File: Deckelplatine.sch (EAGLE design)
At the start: 64 parts, among them IC1 MAX1487EESA+, IC2 74HCT595D, IC3 74HCT595D, IC4 74HCT595D, IC5 74HCT595D, IC6 74HCT595D, J1 52808-2570, U1 LM2676S, X1 236-406/000-023, X2 233-502

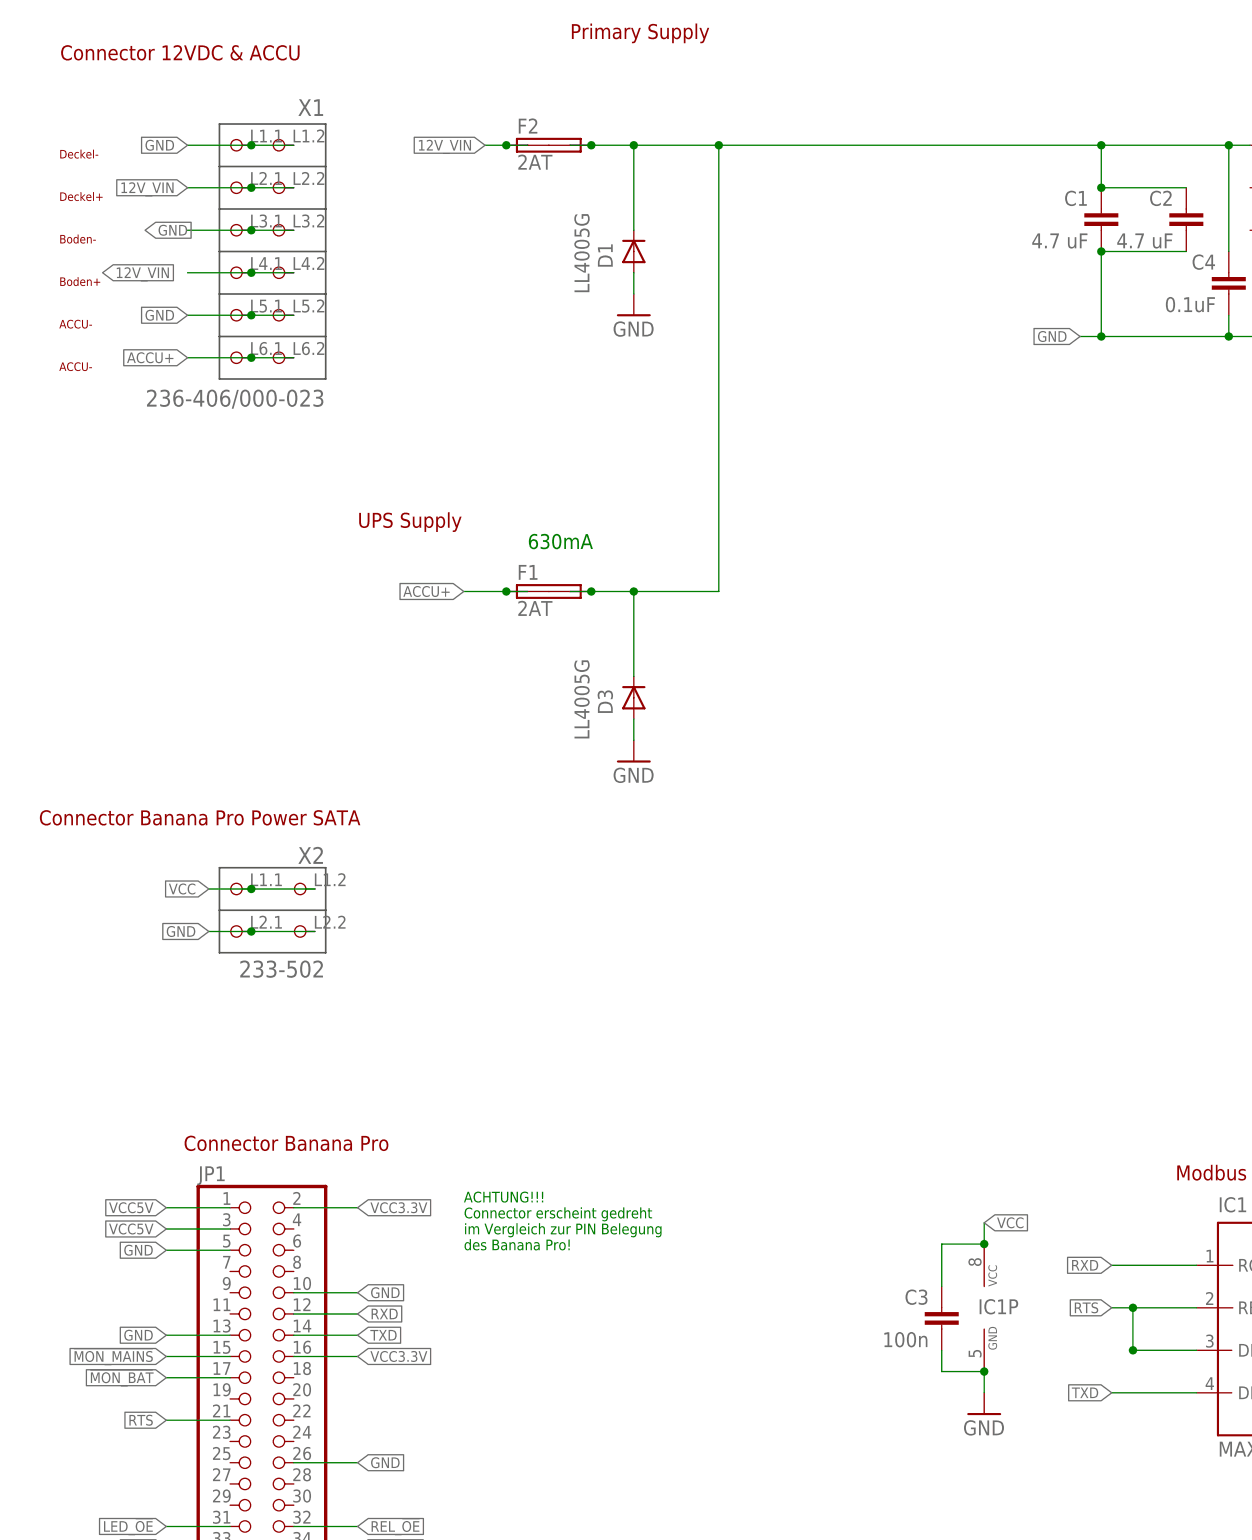
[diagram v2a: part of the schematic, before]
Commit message: BAT und MAINS Monitor
Konnectoren in eigener Bibliothek 'Deckelplatine.lbr'
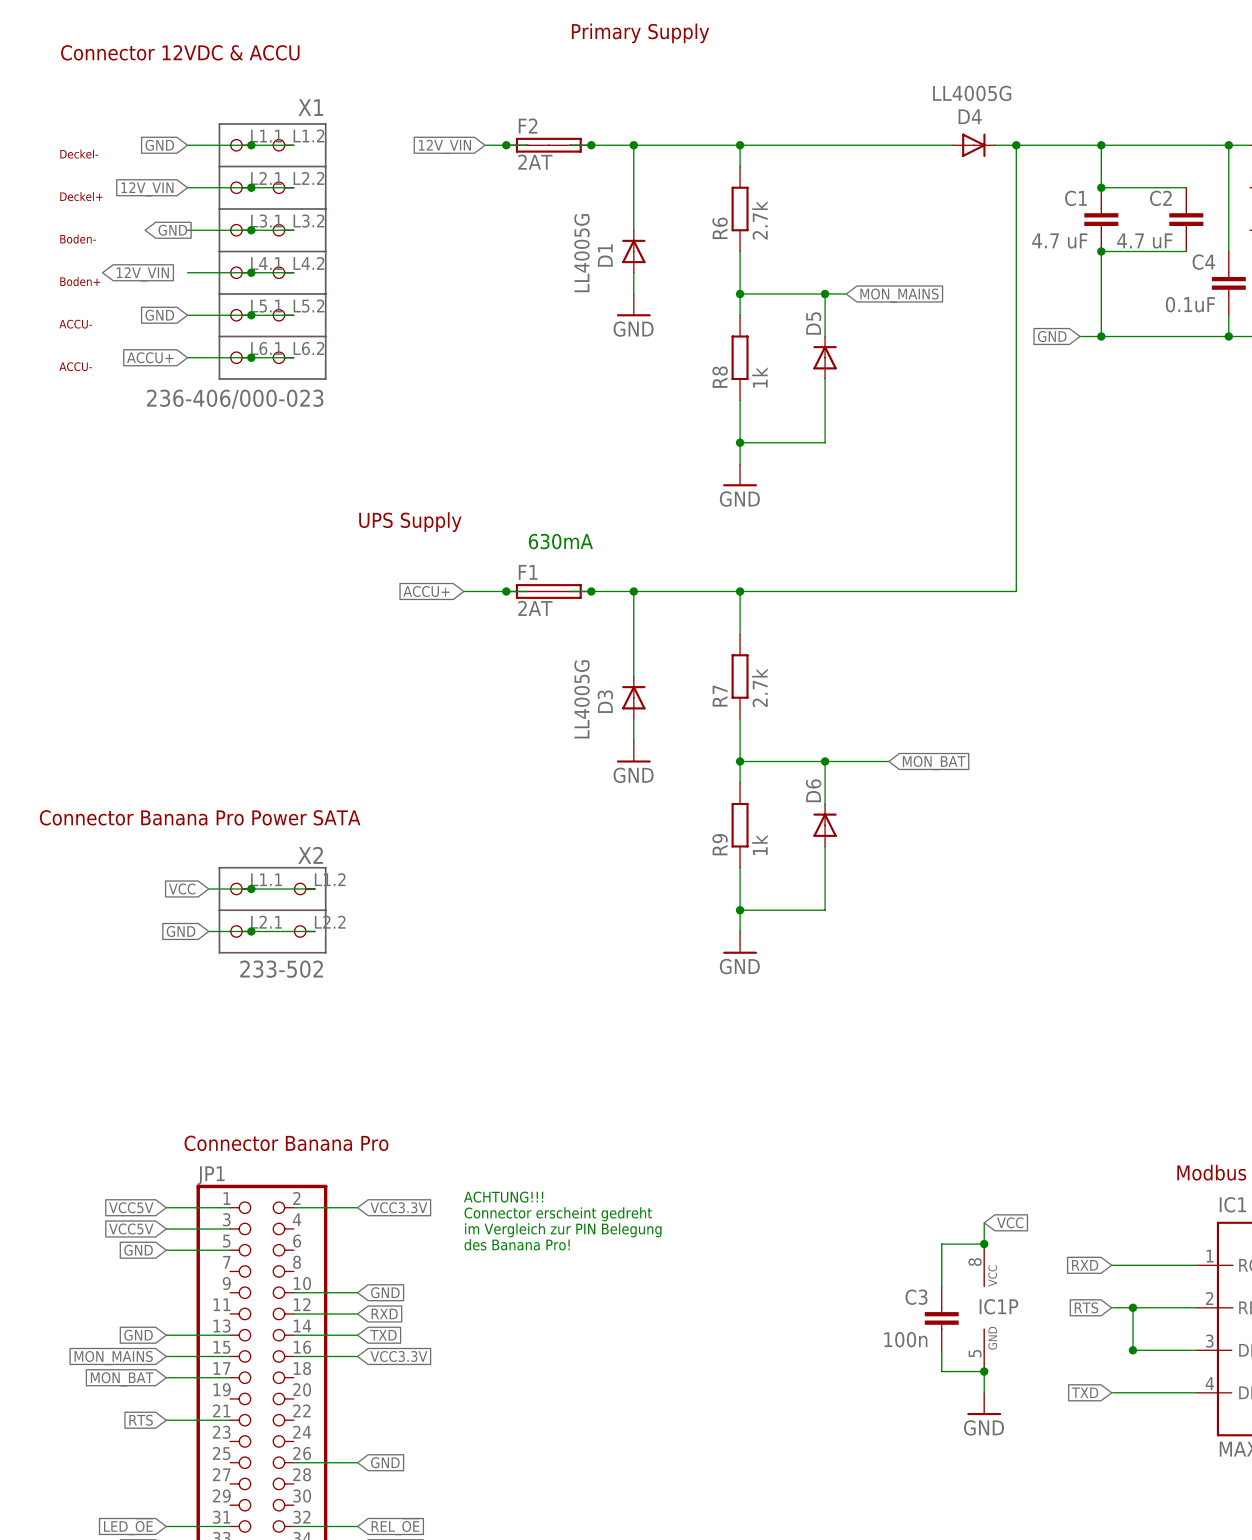
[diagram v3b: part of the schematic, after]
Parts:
- added D4: LL4005G, diode:DIODE-MELF-MLL41
- added D5, D6: (no value), Deckelplatine:DIODE-SOD523
- added R6, R7: 2.7k, RA-GAS Projekte LTD:R-EU_R0603
- added R8, R9: 1k, RA-GAS Projekte LTD:R-EU_R0603
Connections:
- removed net !MON_BAT: JP1.17
- removed net !MON_MAINS: JP1.15
- new net MON_BAT: D6.C, JP1.17, R7.1, R9.2
- new net MON_MAINS: D5.C, JP1.15, R6.1, R8.2
- new net N$37: D1.C, D4.A, F2.2A, F2.2B, R6.2
- net GND: now also D5.A, D6.A, R8.1, R9.1
- net N$4: now also D4.C, R7.2; no longer D1.C, F2.2A, F2.2B

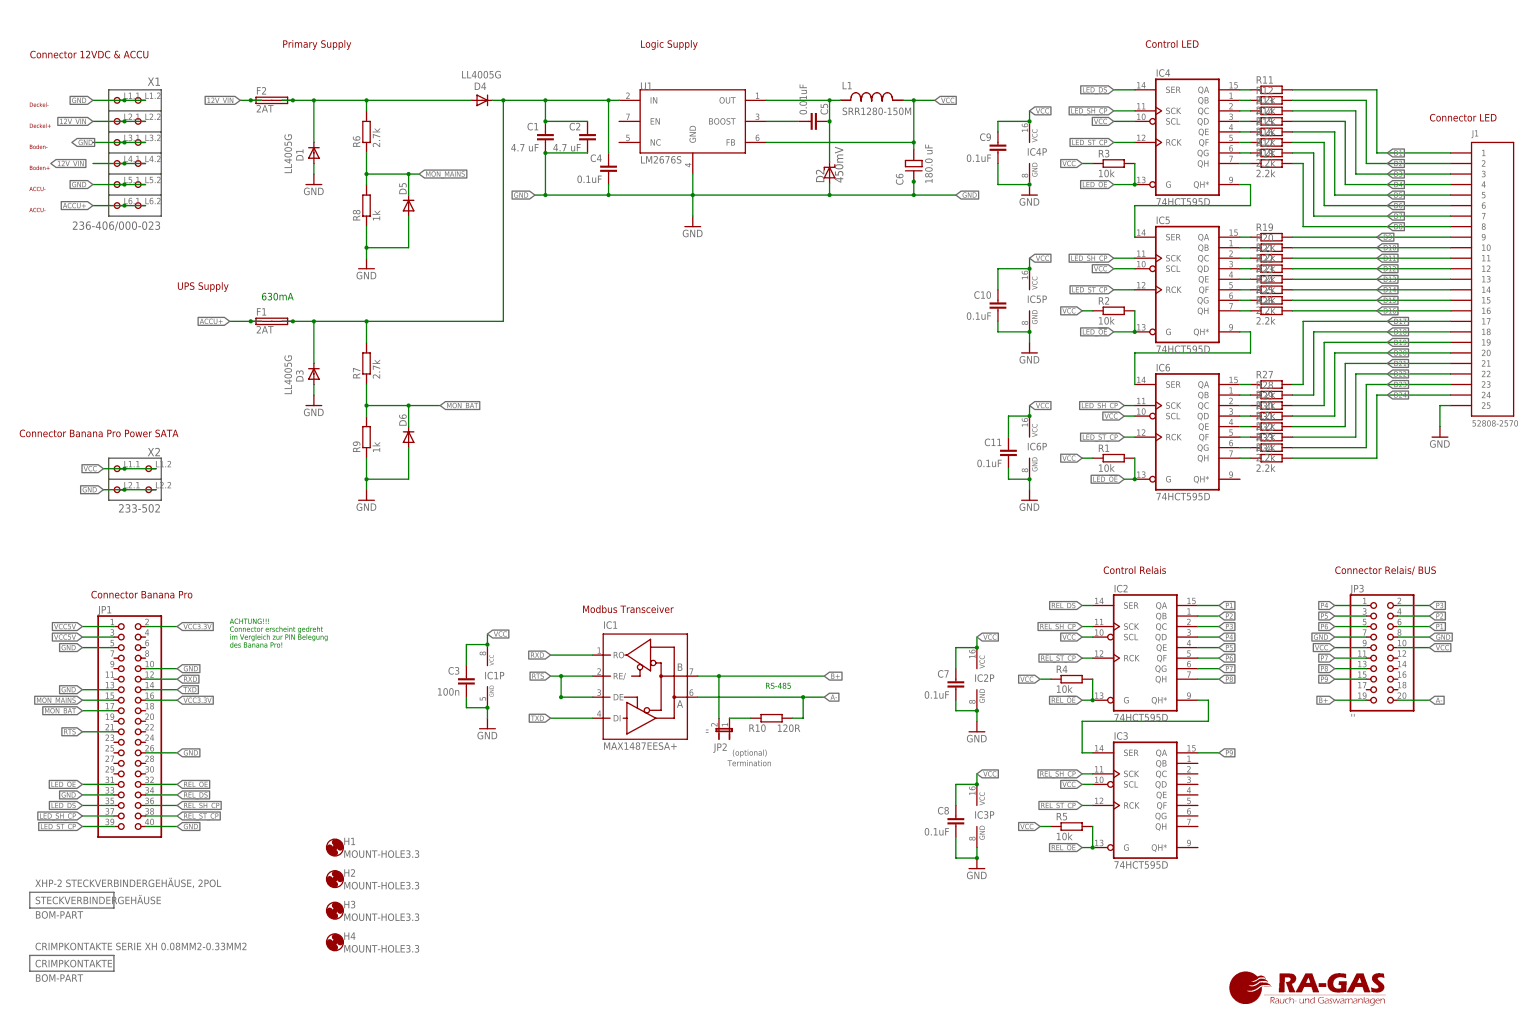
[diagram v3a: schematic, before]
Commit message: Keine Airwire und DRC ist OK
Sparkfun Design-Rule Check ist noch nicht erfüllt, hauptsächlich Winkel der Leiterbahnen und Abstände zu gering.
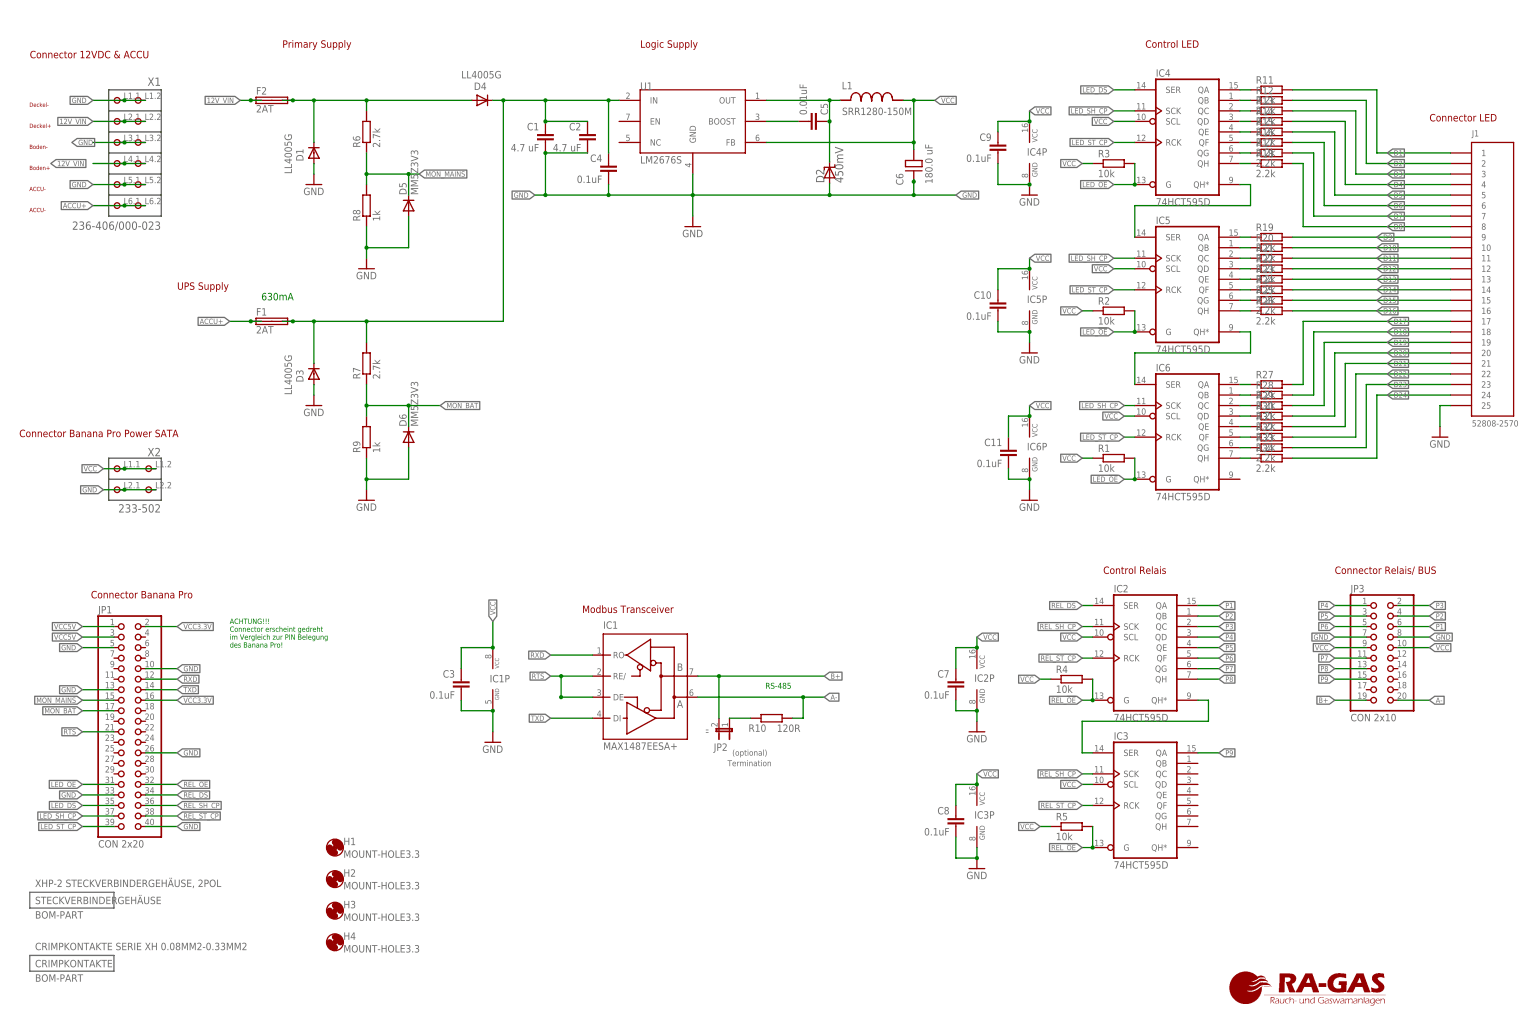
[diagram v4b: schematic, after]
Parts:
- C3: value 100n -> 0.1uF; PARTNO ECHU-16-100N -> SMD TAN.0,1/35
- D5, D6: value (none) -> MM5Z3V3
- JP1: value (none) -> CON 2x20
- JP3: value '' -> CON 2x10; OC_FARNELL_ALTERNATIV 9689621 -> (none); OC_FARNELL_ALTERNATIVE (none) -> 9689621
- X1: DATASHEETURL (none) -> WAGO236_Connector Banana Pro Power SATA-WAGO236-402_WAGO236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
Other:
- moved on the sheet: C3, IC1P
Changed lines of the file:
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@@
 <parts>
 <part name="FRAME1" library="RA-GAS Projekte LTD" deviceset="A3L-LOC-RA-GAS" device="" value="zzeroo systems"/>
-<part name="JP1" library="pinhead" deviceset="PINHD-2X20" device="">
+<part name="JP1" library="pinhead" deviceset="PINHD-2X20" device="" value="CON 2x20">
 <attribute name="DNP" value="T"/>
 <attribute name="MF" value="HARWIN"/>
@@
 <attribute name="OC_FARNELL_ALTERNATIVE" value="1569230"/>
 </part>
-<part name="JP3" library="pinhead" deviceset="PINHD-2X10" device="" value="''">
+<part name="JP3" library="pinhead" deviceset="PINHD-2X10" device="" value="CON 2x10">
 <attribute name="DNP" value="T"/>
 <attribute name="MF" value="TE CONNECTIVITY / AMP"/>
 <attribute name="MPN" value="5103308-5"/>
 <attribute name="OC_FARNELL" value="2452432"/>
-<attribute name="OC_FARNELL_ALTERNATIV" value="9689621"/>
+<attribute name="OC_FARNELL_ALTERNATIVE" value="9689621"/>
 </part>
 <part name="GND4" library="supply1" deviceset="GND" device=""/>
-<part name="C3" library="resistor" deviceset="C-EU" device="C0603" value="100n">
-<attribute name="MF" value="KEMET"/>
-<attribute name="MPN" value="C0603C104K8RACTU"/>
-<attribute name="OC_FARNELL" value="2112833"/>
-<attribute name="PARTNO" value="ECHU-16-100N"/>
-</part>
 <part name="R10" library="rcl" deviceset="R-EU_" device="R1206" value="120R">
 <attribute name="MF" value="TE CONNECTIVITY"/>
@@
 </part>
 <part name="X1" library="con-wago_236" deviceset="236-406/000-023" device="" value="236-406/000-023">
+<attribute name="DATASHEETURL" value="WAGO236_Connector Banana Pro Power SATA-WAGO236-402_WAGO236-403_WAGO236-404#WAG.pdf"/>
 <attribute name="MF" value="WAGO"/>
 <attribute name="MPN" value="236-406"/>
@@
 <attribute name="OC_FARNELL" value="9238484"/>
 </part>
-<part name="D5" library="Deckelplatine" deviceset="DIODE-" device="SOD523">
+<part name="D5" library="Deckelplatine" deviceset="DIODE-" device="SOD523" value=" MM5Z3V3">
 <attribute name="MF" value="FAIRCHILD SEMICONDUCTOR"/>
 <attribute name="MPN" value="MM5Z3V3"/>
@@
 <attribute name="OC_FARNELL" value="9238484"/>
 </part>
-<part name="D6" library="Deckelplatine" deviceset="DIODE-" device="SOD523">
+<part name="D6" library="Deckelplatine" deviceset="DIODE-" device="SOD523" value=" MM5Z3V3">
 <attribute name="MF" value="FAIRCHILD SEMICONDUCTOR"/>
 <attribute name="MPN" value="MM5Z3V3"/>
@@
 <part name="GND3" library="supply1" deviceset="GND" device=""/>
 <part name="GND12" library="supply1" deviceset="GND" device=""/>
+<part name="C3" library="resistor" deviceset="C-EU" device="C0603" value="0.1uF">
+<attribute name="MF" value="KEMET"/>
+<attribute name="MPN" value="C0603C104K8RACTU"/>
+<attribute name="OC_FARNELL" value="2112833"/>
+<attribute name="PARTNO" value="SMD TAN.0,1/35"/>
+</part>
 </parts>
 <sheets>
@@
 </instance>
 <instance part="JP3" gate="A" x="337.82" y="101.6">
-<attribute name="OC_FARNELL_ALTERNATIV" x="337.82" y="101.6" size="1.778" layer="96" display="off"/>
+<attribute name="OC_FARNELL_ALTERNATIVE" x="337.82" y="101.6" size="1.778" layer="96" display="off"/>
 <attribute name="MF" x="337.82" y="101.6" size="1.778" layer="96" display="off"/>
 <attribute name="MPN" x="337.82" y="101.6" size="1.778" layer="96" display="off"/>
@@
 <attribute name="OC_FARNELL" x="337.82" y="101.6" size="1.27" layer="96" display="off"/>
 </instance>
-<instance part="GND4" gate="1" x="123.1646" y="82.0166" smashed="yes">
-<attribute name="VALUE" x="120.6246" y="79.4766" size="1.778" layer="96"/>
-</instance>
-<instance part="C3" gate="G$1" x="118.0846" y="94.7166" smashed="yes" rot="MR0">
-<attribute name="NAME" x="116.5606" y="95.0976" size="1.778" layer="95" rot="MR0"/>
-<attribute name="VALUE" x="116.5606" y="90.0176" size="1.778" layer="96" rot="MR0"/>
-<attribute name="OC_FARNELL" x="118.0846" y="94.7166" size="1.778" layer="96" display="off"/>
-<attribute name="MF" x="118.0846" y="94.7166" size="1.778" layer="96" display="off"/>
-<attribute name="MPN" x="118.0846" y="94.7166" size="1.778" layer="96" display="off"/>
+<instance part="GND4" gate="1" x="124.46" y="78.74" smashed="yes">
+<attribute name="VALUE" x="121.92" y="76.2" size="1.778" layer="96"/>
 </instance>
 <instance part="R10" gate="G$1" x="191.7446" y="84.5566" smashed="yes">
@@
 <attribute name="VALUE" x="151.1046" y="76.9366" size="1.778" layer="96"/>
 </instance>
-<instance part="IC1" gate="P" x="123.1646" y="94.7166"/>
+<instance part="IC1" gate="P" x="124.46" y="93.98"/>
 <instance part="JP2" gate="A" x="181.5846" y="82.0166" smashed="yes" rot="R180">
 <attribute name="NAME" x="177.7746" y="76.6826" size="1.778" layer="95"/>
@@
 <attribute name="MF" x="38.1" y="220.98" size="1.27" layer="96" display="off"/>
 <attribute name="MPN" x="38.1" y="220.98" size="1.27" layer="96" display="off"/>
+<attribute name="DATASHEETURL" x="38.1" y="220.98" size="1.27" layer="96" rot="MR0" display="off"/>
 </instance>
 <instance part="X2" gate="G$1" x="38.1" y="142.24" rot="MR0">
@@
 <attribute name="VALUE" x="91.44" y="134.62" size="1.778" layer="96"/>
 </instance>
+<instance part="C3" gate="G$1" x="116.84" y="93.98" smashed="yes" rot="MR0">
+<attribute name="NAME" x="115.316" y="94.361" size="1.778" layer="95" rot="MR0"/>
+<attribute name="VALUE" x="115.316" y="89.281" size="1.778" layer="96" rot="MR0"/>
+<attribute name="OC_FARNELL" x="116.84" y="93.98" size="1.778" layer="96" display="off"/>
+<attribute name="MF" x="116.84" y="93.98" size="1.778" layer="96" display="off"/>
+<attribute name="MPN" x="116.84" y="93.98" size="1.778" layer="96" display="off"/>
+</instance>
 </instances>
 <busses>
@@
 <pinref part="IC1" gate="P" pin="GND"/>
 <pinref part="GND4" gate="1" pin="GND"/>
-<wire x1="123.1646" y1="87.0966" x2="123.1646" y2="84.5566" width="0.1524" layer="91"/>
+<wire x1="124.46" y1="86.36" x2="124.46" y2="81.28" width="0.1524" layer="91"/>
 <pinref part="C3" gate="G$1" pin="2"/>
-<wire x1="118.0846" y1="89.6366" x2="118.0846" y2="87.0966" width="0.1524" layer="91"/>
-<wire x1="118.0846" y1="87.0966" x2="123.1646" y2="87.0966" width="0.1524" layer="91"/>
-<junction x="123.1646" y="87.0966"/>
+<wire x1="116.84" y1="88.9" x2="116.84" y2="86.36" width="0.1524" layer="91"/>
+<wire x1="116.84" y1="86.36" x2="124.46" y2="86.36" width="0.1524" layer="91"/>
+<junction x="124.46" y="86.36"/>
 </segment>
 <segment>
@@
 <segment>
 <pinref part="IC1" gate="P" pin="VCC"/>
+<wire x1="124.46" y1="101.6" x2="124.46" y2="107.9246" width="0.1524" layer="91"/>
+<label x="124.46" y="107.9246" size="1.27" layer="95" rot="R90" xref="yes"/>
 <pinref part="C3" gate="G$1" pin="1"/>
-<wire x1="118.0846" y1="97.2566" x2="118.0846" y2="102.3366" width="0.1524" layer="91"/>
-<wire x1="118.0846" y1="102.3366" x2="123.1646" y2="102.3366" width="0.1524" layer="91"/>
-<wire x1="123.1646" y1="102.3366" x2="123.1646" y2="104.8766" width="0.1524" layer="91"/>
-<junction x="123.1646" y="102.3366"/>
-<label x="123.1646" y="104.8766" size="1.27" layer="95" xref="yes"/>
-</segment>
-<segment>
+<wire x1="116.84" y1="96.52" x2="116.84" y2="101.6" width="0.1524" layer="91"/>
+<wire x1="116.84" y1="101.6" x2="124.46" y2="101.6" width="0.1524" layer="91"/>
+<junction x="124.46" y="101.6"/>
+</segment>
+<segment>
